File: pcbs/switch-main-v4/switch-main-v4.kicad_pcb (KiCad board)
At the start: 6 copper layers, 65 x 50 mm, 481 parts, among them J2401 JST-GH-2-Horizontal, J2402 JST-GH-2-Horizontal, J2403 MSPE-J2L0-B00, J2404 MSPE-J2L0-B00, J2405 MSPE-J2L0-x00, J301 MKXS1-1 Power Input, J601 MKXS1-1 Power Input, Q1101 DMN21D2UFB-7B, Q1102 DMN21D2UFB-7B, Q1103 DMN21D2UFB-7B, Q1301 DMN21D2UFB-7B, Q1302 DMP21D0UFB-7B, Q1401 DMN21D2UFB-7B, Q1402 DMP21D0UFB-7B, Q1501 DMN21D2UFB-7B, Q1502 DMP21D0UFB-7B, Q2201 DMP21D0UFB-7B, Q2202 DMP21D0UFB-7B, Q2203 DMN21D2UFB-7B, Q2204 DMP21D0UFB-7B, Q2205 DMN21D2UFB-7B, Q2206 DMP21D0UFB-7B, Q2301 DMN21D2UFB-7B, Q2302 DMP21D0UFB-7B, Q2601 DMN21D2UFB-7B, Q2602 DMN21D2UFB-7B, Q801 DMP21D0UFB-7B, T1801 74930100, T1901 74930100, T2001 74930100, T2101 74930100, U1201 LMK1C1104DQFR, U1301 TPS62290TDRVRQ1, U1302 88Q2112-A2-NYD2A000-P123, U1401 TPS62290TDRVRQ1, U1402 88Q2112-A2-NYD2A000-P123, U1501 TPS62290TDRVRQ1, U1502 88Q2112-A2-NYD2A000-P123, U1601 LAN8671C2-E_U3B, U2201 TPS27S100BRRK, U2202 TPS27S100BRRK, U2301 NCS213RMUTAG, U2302 TPS27S100BRRK, U2501 ISO6521REUR, U2502 ISO6520REUR, U2601 STM32H503KBUx, U301 TVS3301DRBR, U302 TPS26600RHFR, U401 TPS7B8133QDRVRQ1, U402 LMQ66420MC3RXBRQ1, U403 TPS2116DRL, U501 TPS62290TDRVRQ1, U502 TPS62290TDRVRQ1, U601 TVS3301DRBR, U602 TPS26600RHFR, U701 TPS7B8133QDRVRQ1, U702 MAX20075DATCA/V+, U703 NCP508MT25TBG, U801 FM25CL64B-DG, U802 STM32H573IIKxQ, U901 SJA1105QELY, Y801 XRCGB25M000F3A16R0, Y802 ECS-.327-7-12QS-TR, Y901 XRCGB25M000F3A16R0

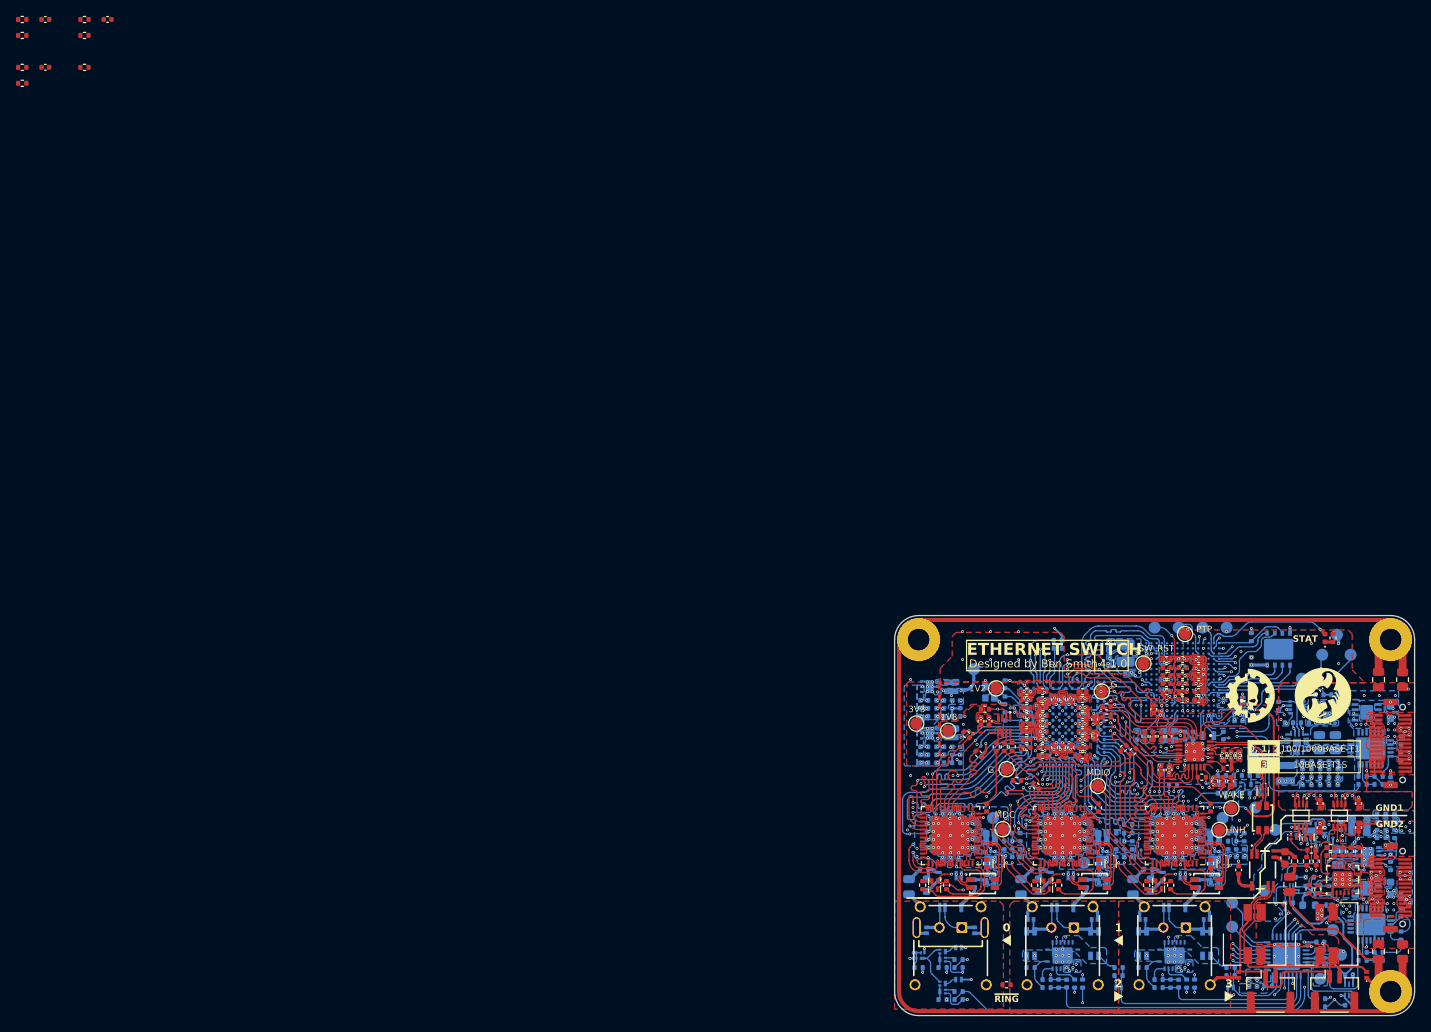
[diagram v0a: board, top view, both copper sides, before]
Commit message: Updated to Kicad v10
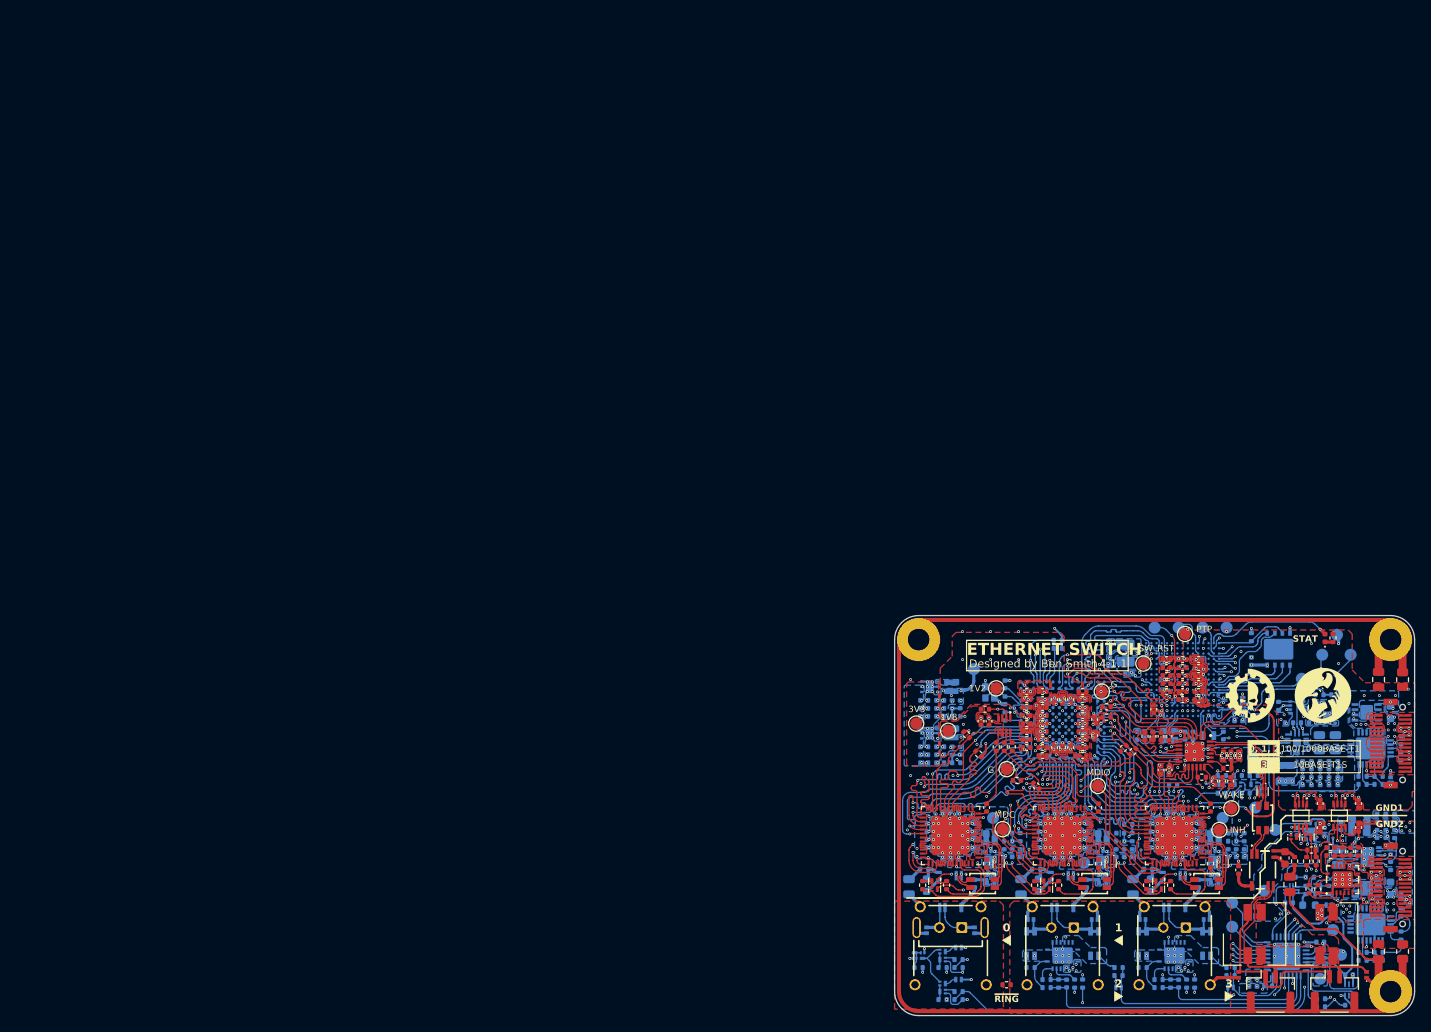
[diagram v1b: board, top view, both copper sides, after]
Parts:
- removed C1322, C1422, C1522: 10u, project_footprints:C_0402
- removed R1302, R1402, R1502, R1603: 10k, project_footprints:R_0402
- removed R1304, R1404, R1504: 4k7, project_footprints:R_0402
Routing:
- net GND1: track 92.7 -> 95.0 mm
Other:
- board text added: "26/04/2026"
- board text added: "4.1.1"
- board text removed: "07/08/2025"
- board text removed: "4.1.0"
